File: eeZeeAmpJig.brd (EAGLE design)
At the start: 31 x 20.6 mm, 18 parts

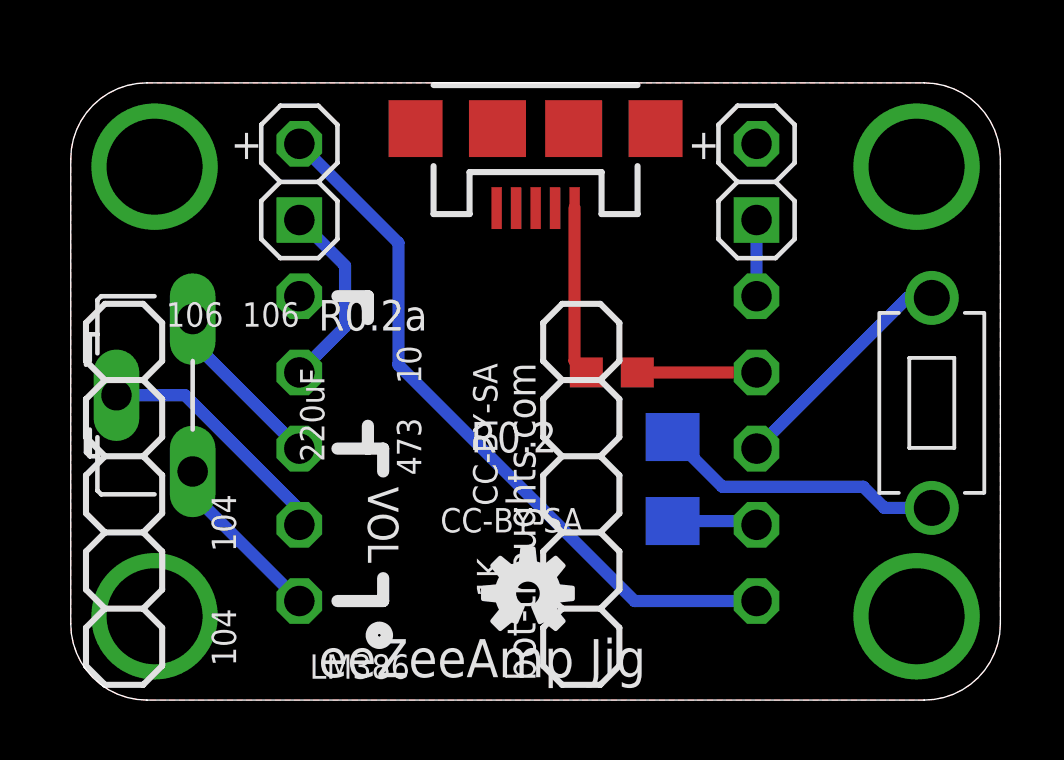
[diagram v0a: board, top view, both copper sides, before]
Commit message: Altered gain to 40.5 with resistor, changed pot value, created silk and gerbers
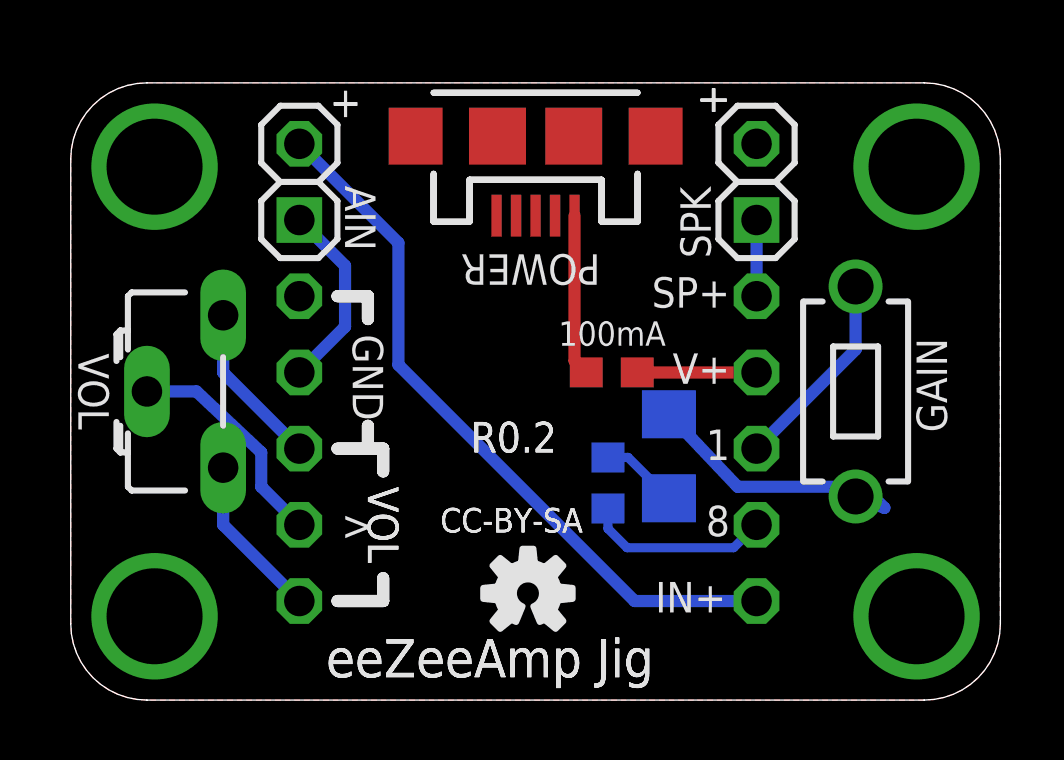
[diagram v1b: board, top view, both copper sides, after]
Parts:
- added R1: 1K, rcl:R0603
- JP14: value SPKR -> SPK
- R2: value VOL -> 100K
- moved S2 2.57 mm to (26.2, 10.3)
- moved R2 1.02 mm to (5.08, 10.3)
- moved C1 0.77 mm to (19.9, 8.13)
- moved JP11 0.25 mm to (15.5, 18.8)
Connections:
- new net N$5: C1.2, R1.1
- net 8: now also R1.2; no longer C1.2
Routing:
- net 8: track 2.84 -> 6.21 mm
- net N$5: track 0.00 -> 2.60 mm
- net N$1: track 7.92 -> 6.77 mm
- net 3: track 8.18 -> 7.55 mm
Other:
- board text added: "100mA"
- board text added: "AIN"
- board text added: "POWER"
- board text added: "SPK"
- board text removed: "10"
- board text removed: "104"
- board text removed: "220uF"
- board text removed: "473"
- board text removed: "LM386"
- board text removed: "R0.2a"
- board text removed: "eeZeeAmp"

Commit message: increased switch/pot clearance by embiggening board. Moved fuse to bottom layer. Changed some silk
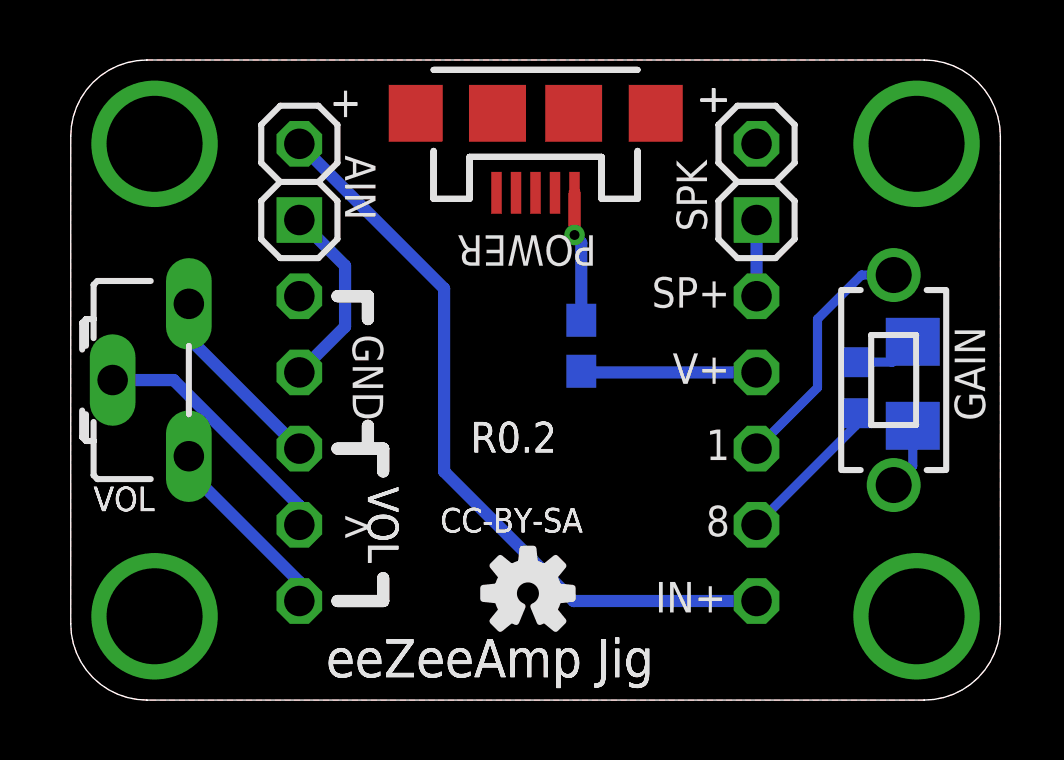
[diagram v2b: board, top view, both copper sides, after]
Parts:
- moved R1 8.84 mm to (26.2, 10.4)
- moved C1 8.48 mm to (28.1, 10.5), turned to 90 degrees
- moved F1 1.35 mm to (17.0, 11.8), flipped to the bottom, turned to 270 degrees
- moved S2 1.33 mm to (27.4, 10.7)
- moved R2 1.20 mm to (3.94, 10.7)
- moved JP11 0.76 mm to (15.5, 19.6)
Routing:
- net 1: track 9.55 -> 2.24 mm
- net N$4: track 3.98 -> 5.85 mm
- net N$1: track 6.77 -> 8.31 mm
- net AUDIO_IN: track 23.9 -> 25.1 mm
- net 8: track 6.21 -> 5.09 mm
- net VCC: track 5.39 -> 4.33 mm, vias 0 -> 1
- net 3: track 7.55 -> 8.59 mm
- net N$8: track 5.50 -> 6.35 mm
- net N$3: track 5.50 -> 6.35 mm
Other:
- board size 31 x 20.6 mm -> 31 x 21.3 mm
- board text added: "100K"

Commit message: increased drill size for pogos, replaced microB with pin headers, moved power, ain, spkr pin headers, shrank board, centered pogo pin test area, reduced mounting hole drill size to #2, reduced spacer tdocu circles to actual for #2 size screws, changed switch to smaller smt version
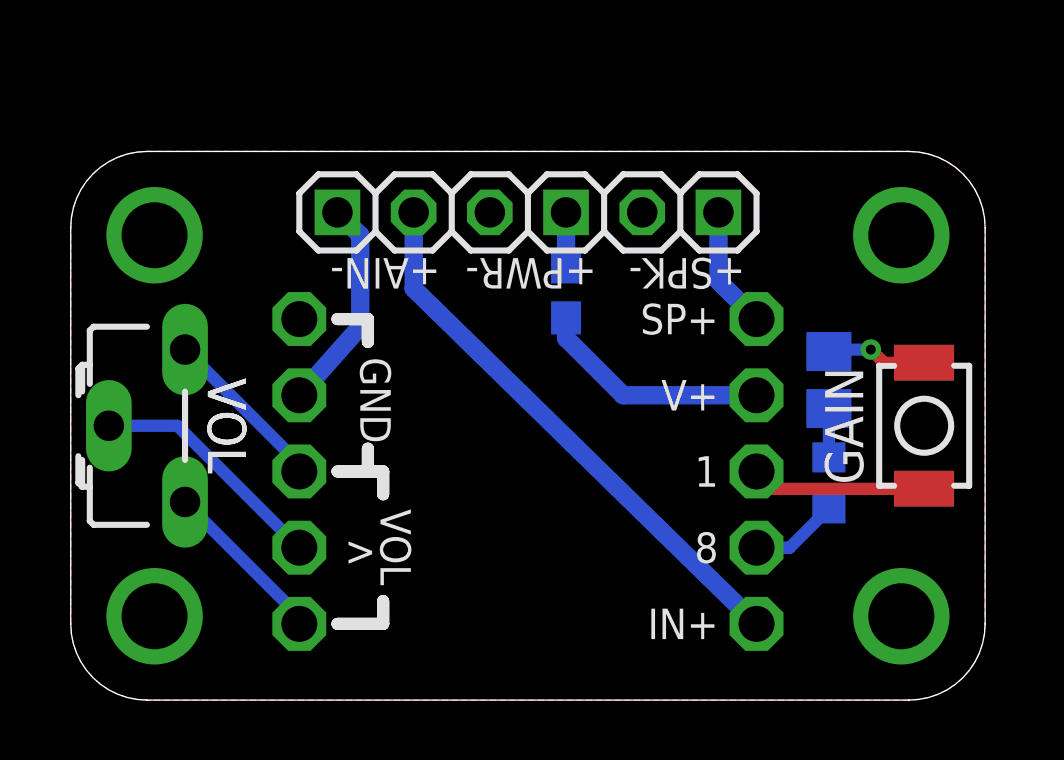
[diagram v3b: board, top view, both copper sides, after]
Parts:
- removed JP10: IN-, pinhead-2:1X01-S
- removed JP11: POWER, SparkFun-Connectors:USB-MICROB
- removed JP2: >, pinhead-2:1X01-S
- removed JP3: 1, pinhead-2:1X01-S
- removed JP4: VR-, pinhead-2:1X01-S
- removed JP5: IN+, pinhead-2:1X01-S
- removed JP6: V+, pinhead-2:1X01-S
- removed JP7: SP+, pinhead-2:1X01-S
- removed JP8: 8, pinhead-2:1X01-S
- removed JP9: VR+, pinhead-2:1X01-S
- added PAD1: V+, bt_electromech:POGO_1.02MM
- added PAD10: SP+, bt_electromech:POGO_1.02MM
- added PAD11: IN-, bt_electromech:POGO_1.02MM
- added PAD12: IN+, bt_electromech:POGO_1.02MM
- added PAD2: GND, bt_electromech:POGO_1.02MM
- added PAD3, PAD5: VOL, bt_electromech:POGO_1.02MM
- added PAD4: >, bt_electromech:POGO_1.02MM
- added PAD8: 1, bt_electromech:POGO_1.02MM
- added PAD9: 8, bt_electromech:POGO_1.02MM
- C1: device rcl:C1206 -> rcl:C0805
- JP1: value GND -> +PWR-; device pinhead-2:1X01-S -> pinhead-2:1X02-S
- JP14: value SPK -> +SPK-
- JP15: value AIN -> +AIN-
- S2: device bt_electromech:6MMTACTILE_RECT -> bt_electromech:3X4X2TACT
- moved JP1 8.12 mm to (15.2, 16.3), flipped to the top, turned to 180 degrees
- moved LOGO2 6.73 mm to (15.2, 10.3), flipped to the bottom
- moved R1 3.30 mm to (25.3, 7.24)
- moved C1 2.80 mm to (25.3, 10.7), turned to 270 degrees
- moved JP14 2.74 mm to (20.3, 16.3), turned to 180 degrees
- moved JP15 2.74 mm to (10.2, 16.3), turned to 0 degrees
- moved F1 1.85 mm to (16.5, 13.6)
- moved S2 1.83 mm to (28.4, 9.14), turned to 270 degrees
- moved R2 1.53 mm to (3.81, 9.14)
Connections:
- removed net AUDIO_IN: JP15.2, JP5.1
- removed net N$2: JP10.1, JP15.1
- new net IN+: JP15.2, PAD12.P$1
- new net IN-: JP15.1, PAD11.P$1
- net 3: now also PAD4.P$1; no longer JP2.1
- net 8: now also PAD9.P$1; no longer JP8.1
- net GND: now also JP1.2, PAD2.P$1; no longer JP1.1, JP11.GND, JP11.MT1, JP11.MT2
- net N$1: now also PAD8.P$1; no longer JP3.1
- net N$3: now also PAD5.P$1; no longer JP4.1
- net N$4: now also PAD1.P$1; no longer JP6.1
- net N$8: now also PAD3.P$1; no longer JP9.1
- net SPEAKER: now also PAD10.P$1; no longer JP7.1
- net VCC: now also JP1.1; no longer JP11.VBUS
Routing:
- net AUDIO_IN: track 25.1 -> 0.00 mm
- net IN+: track 0.00 -> 18.5 mm
- net IN-: track 0.00 -> 7.18 mm
- net N$2: track 6.34 -> 0.00 mm
- net VCC: track 4.33 -> 1.82 mm, vias 1 -> 0
- net N$1: track 8.31 -> 5.83 mm
- net 8: track 5.09 -> 2.96 mm
- net N$4: track 5.85 -> 7.81 mm
- net SPEAKER: track 2.54 -> 4.08 mm
- net 1: track 2.24 -> 3.38 mm, vias 0 -> 1
- net N$3: track 6.35 -> 5.64 mm
- net N$8: track 6.35 -> 5.64 mm
- net 3: track 8.59 -> 8.03 mm
- net N$5: track 2.19 -> 1.63 mm
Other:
- board size 31 x 21.3 mm -> 30.5 x 18.3 mm
- board text added: "+AIN-"
- board text added: "+PWR-"
- board text added: "+SPK-"
- board text added: "R0.3"
- board text removed: "+"
- board text removed: "AIN"
- board text removed: "POWER"
- board text removed: "R0.2"
- board text removed: "SPK"
